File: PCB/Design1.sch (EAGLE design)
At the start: 23 parts, among them J1 FTDI_DEVICE, U1 ATMEGA2560AU

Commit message: Update new Schematic
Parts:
- added CHARGE: (no value), SparkFun-Connectors:M03X2FEMALE
- added D2: (no value), SparkFun-DiscreteSemi:DIODESMA-ALT
- added R4: 470KΩ, SparkFun-Resistors:RESISTOR1206
- added R5: 100KΩ, SparkFun-Resistors:RESISTOR1206
- 5V: value 7805T -> 7805
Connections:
- net SERIAL0 renamed TX1
- net SERIAL1 renamed RX1
- net SERIAL2 renamed TX2
- net SERIAL3 renamed RX2
- new net RAW: D2.A, POWER.2
- new net VSENSE: R4.2, R5.1
- net GND: now also CHARGE.2, CHARGE.6, R5.2
- net VIN: now also D2.C, R4.1; no longer POWER.2
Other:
- note added: "Power Source Mgmt"
- moved on the sheet: 5V, C1, C2, C6, POWER

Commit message: last nights' Schematic updates
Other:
- note added: "Reset circuitry"
- moved on the sheet: 5V, AMS1117, C1, C10, C2, C3, C4, C5, C6, C9, D1, D2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

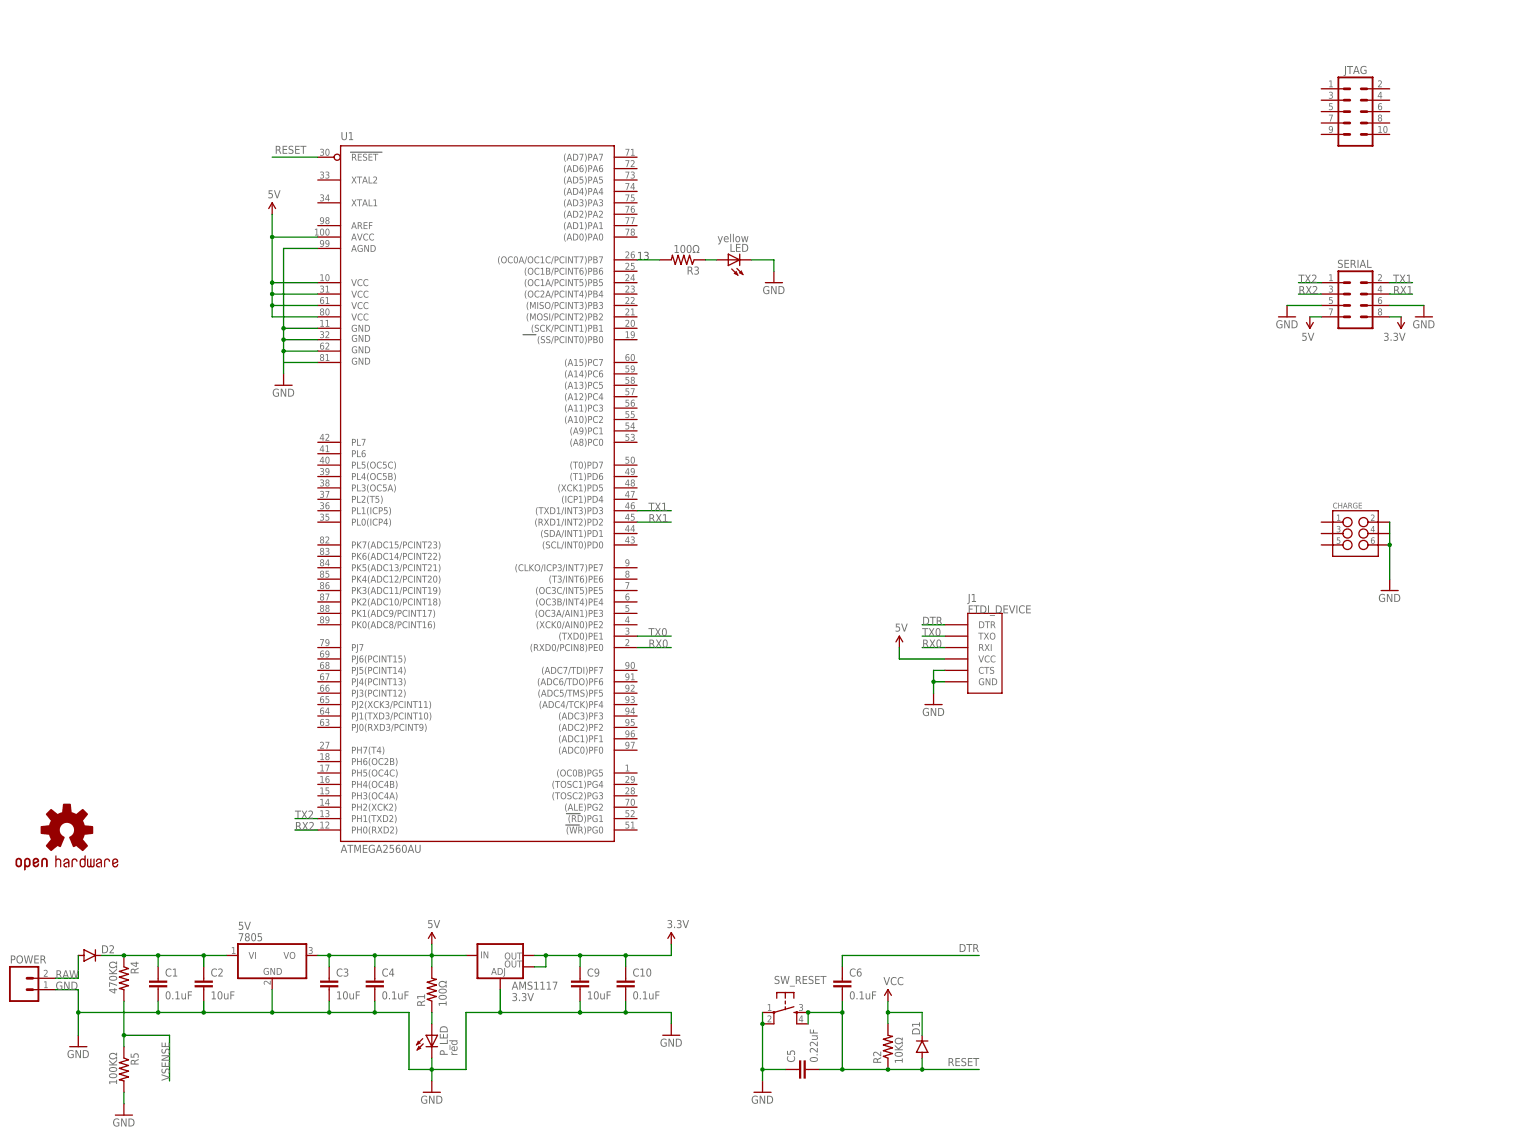
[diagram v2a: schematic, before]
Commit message: Add ICSP & Organize LEDs
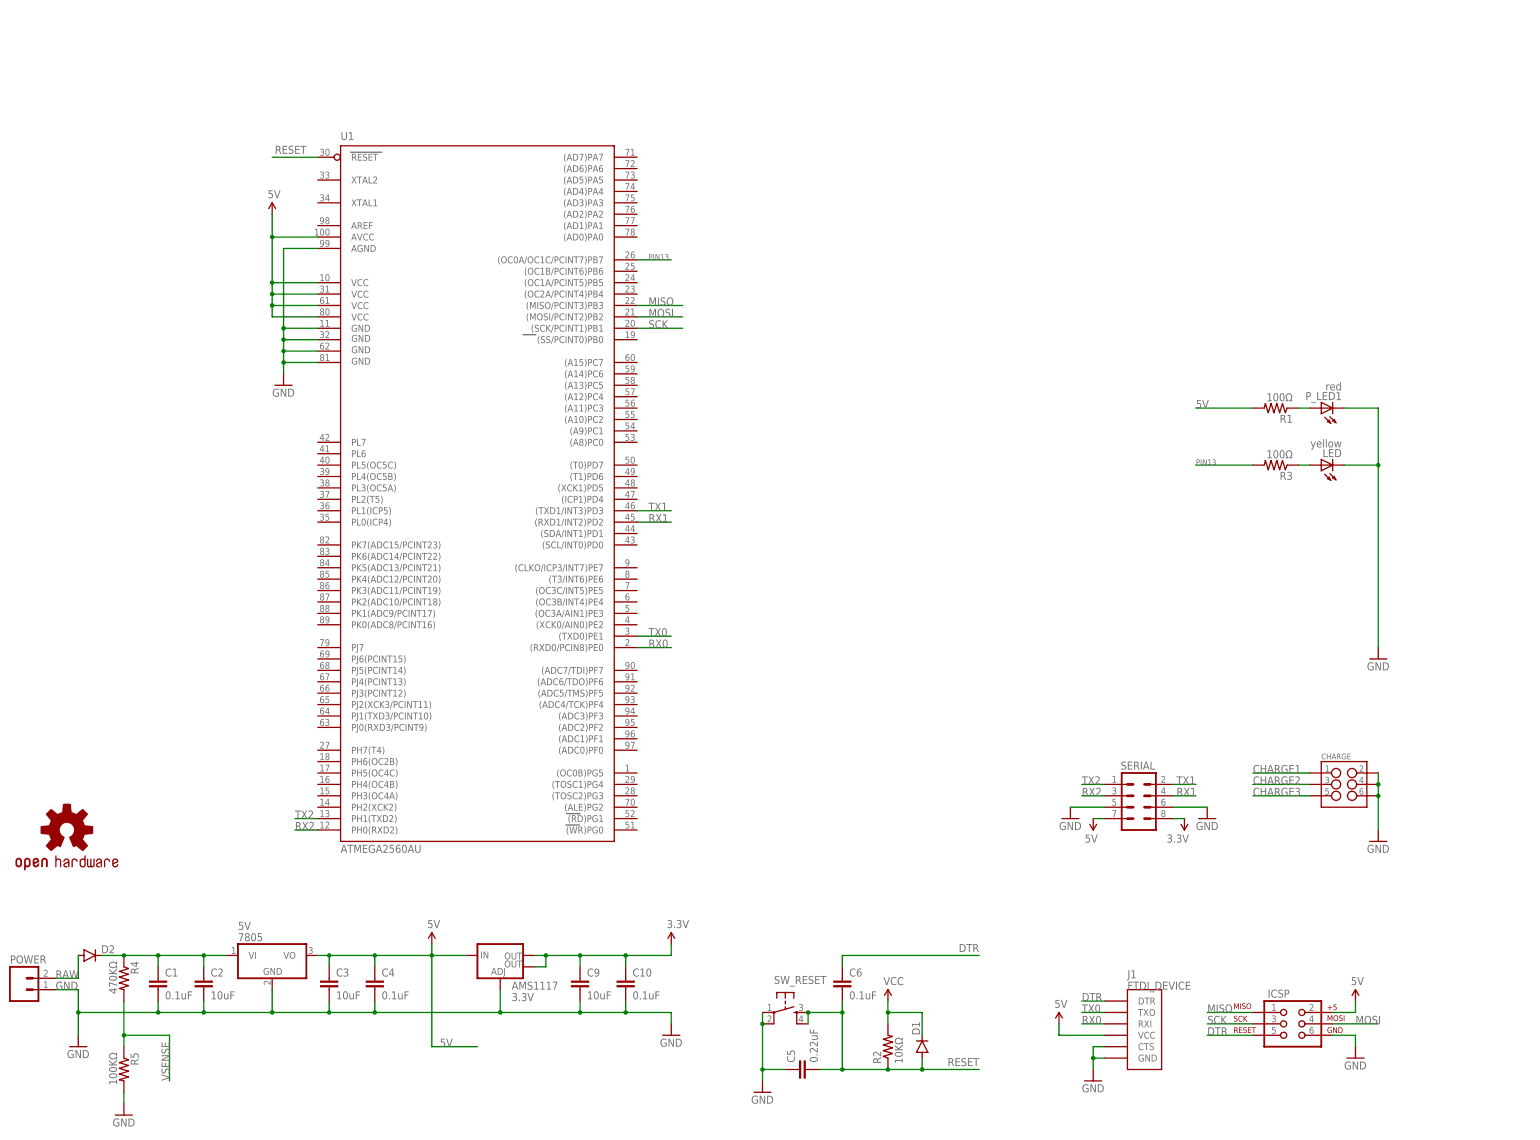
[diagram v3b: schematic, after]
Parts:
- removed JTAG: (no value), SparkFun-Connectors:M05X2PTH
- removed P_LED: red, led:LEDSML0805
- added ICSP: AVR_SPI_PRG_6PTH, SparkFun-Connectors:AVR_SPI_PRG_6PTH
- added P_LED1: red, led:LEDSML0805
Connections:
- removed net N$1: P_LED.A, R1.1
- new net CHARGE1: CHARGE.1
- new net CHARGE2: CHARGE.3
- new net CHARGE3: CHARGE.5
- new net MISO: ICSP.1, U1.(MISO/PCINT3)PB3
- new net MOSI: ICSP.4, U1.(MOSI/PCINT2)PB2
- new net N$2: P_LED1.A, R1.1
- new net SCK: ICSP.3, U1.(SCK/PCINT1)PB1
- net 5V: now also ICSP.2
- net DTR: now also ICSP.5
- net GND: now also CHARGE.4, ICSP.6, P_LED1.C; no longer P_LED.C
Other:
- note added: "(LED)"
- note added: "LEDs"
- note added: "Peripheral Connections"
- note added: "Programming Connections"
- note removed: "13"
- moved on the sheet: CHARGE, J1, LED, R1, R3, SERIAL

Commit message: Ad LEDS, begin work on MOSFETs
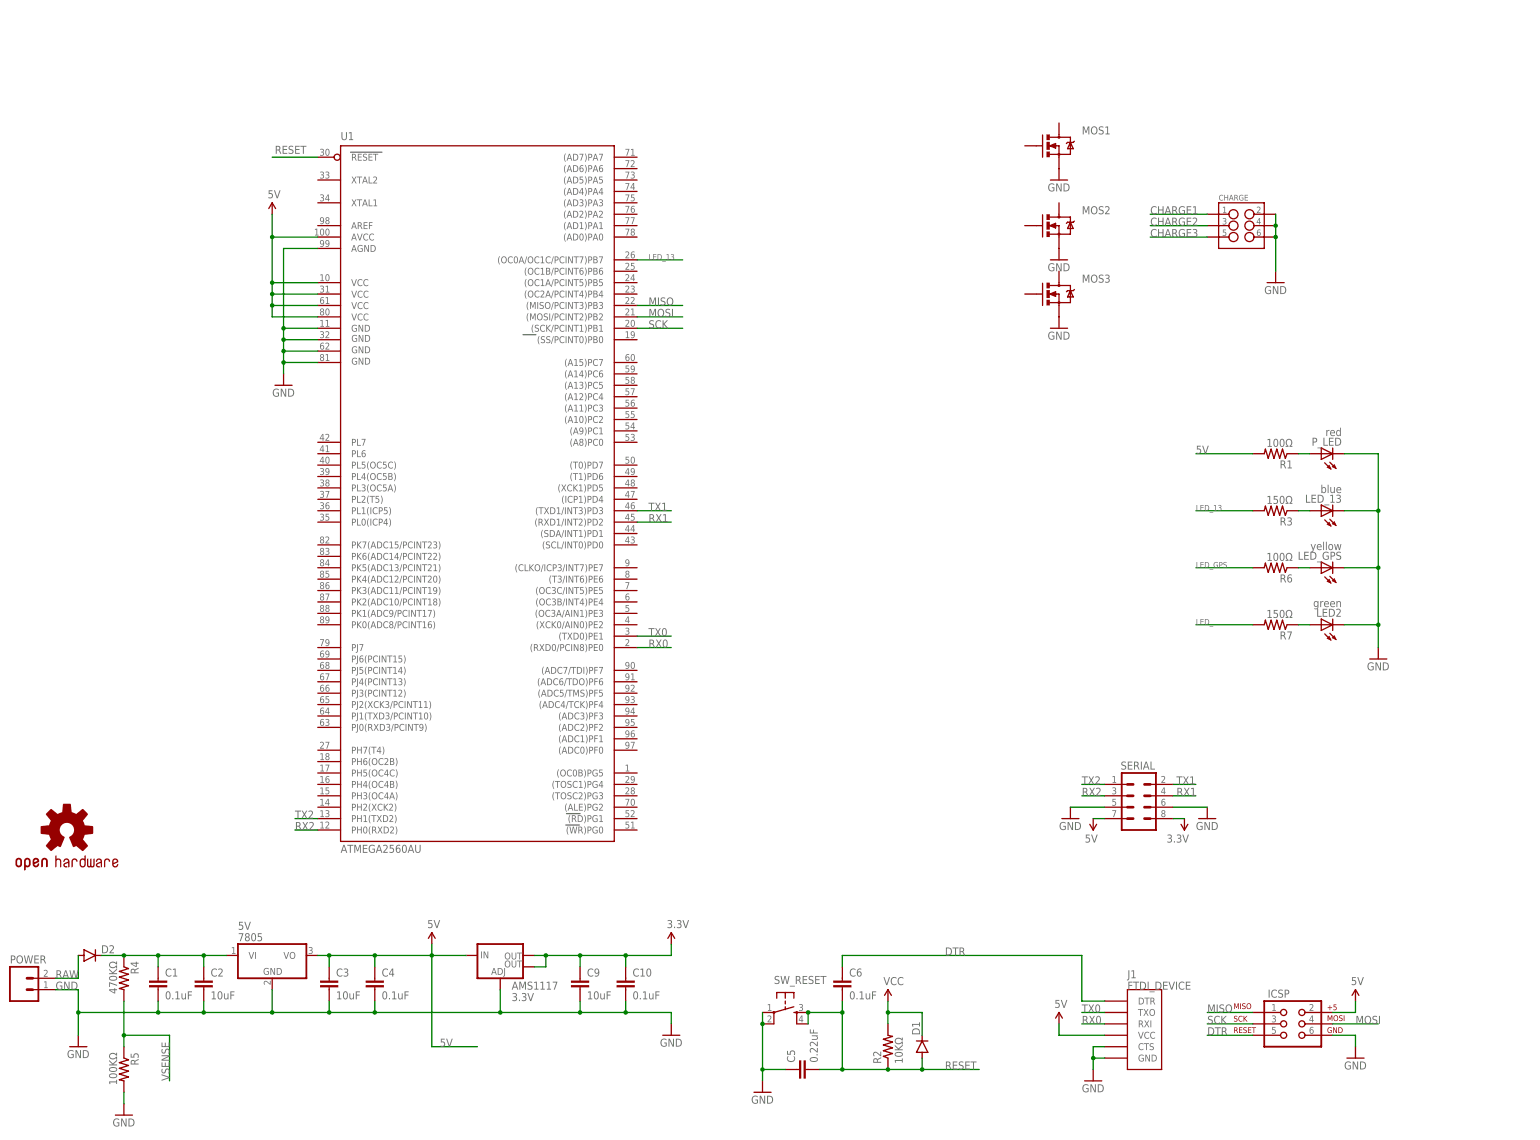
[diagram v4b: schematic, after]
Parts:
- removed LED: yellow, led:LEDSML0805
- removed P_LED1: red, led:LEDSML0805
- added LED2: green, led:LEDSML0805
- added LED_13: blue, led:LEDSML0805
- added LED_GPS: yellow, led:LEDSML0805
- added MOS1, MOS2, MOS3: MOSFET-NCHANNELFQP30N06L, SparkFun-DiscreteSemi:MOSFET-NCHANNELFQP30N06L
- added P_LED: red, led:LEDSML0805
- added R6: 100Ω, SparkFun-Resistors:RESISTOR1206
- added R7: 150Ω, SparkFun-Resistors:RESISTOR1206
- R3: value 100Ω -> 150Ω
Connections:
- net PIN13 renamed LED_13
- new net LED_: R7.2
- new net LED_GPS: R6.2
- new net N$1: LED_GPS.A, R6.1
- new net N$4: LED2.A, R7.1
- net GND: now also LED2.C, LED_13.C, LED_GPS.C, MOS1.S, MOS2.S, MOS3.S, P_LED.C; no longer LED.C, P_LED1.C
- net N$2: now also P_LED.A; no longer P_LED1.A
- net N$3: now also LED_13.A; no longer LED.A
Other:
- moved on the sheet: CHARGE, R1, R3

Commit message: Place mosfets
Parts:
- removed CHARGE: (no value), SparkFun-Connectors:M03X2FEMALE
- removed MOS3: MOSFET-NCHANNELFQP30N06L, SparkFun-DiscreteSemi:MOSFET-NCHANNELFQP30N06L
- added J2, J3: (no value), SparkFun-Connectors:M02LOCK_LONGPADS
- added R8, R9: 10KΩ, SparkFun-Resistors:RESISTOR1206
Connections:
- removed net CHARGE3: CHARGE.5
- removed net RAW: D2.A, POWER.2
- new net MOS1: J2.1, MOS1.D
- new net MOS2: J3.1, MOS2.D
- new net N$8: 5V.VI, C1.1, C2.1, D2.C, R4.1
- net CHARGE1: now also MOS1.G, R8.1; no longer CHARGE.1
- net CHARGE2: now also MOS2.G, R9.1; no longer CHARGE.3
- net GND: now also R8.2, R9.2; no longer CHARGE.2, CHARGE.4, CHARGE.6, MOS3.S
- net VIN: now also D2.A, J2.2, J3.2, POWER.2; no longer 5V.VI, C1.1, C2.1, D2.C, R4.1
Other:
- note added: "'Charge' MOSFET Switching"
- moved on the sheet: MOS1, MOS2

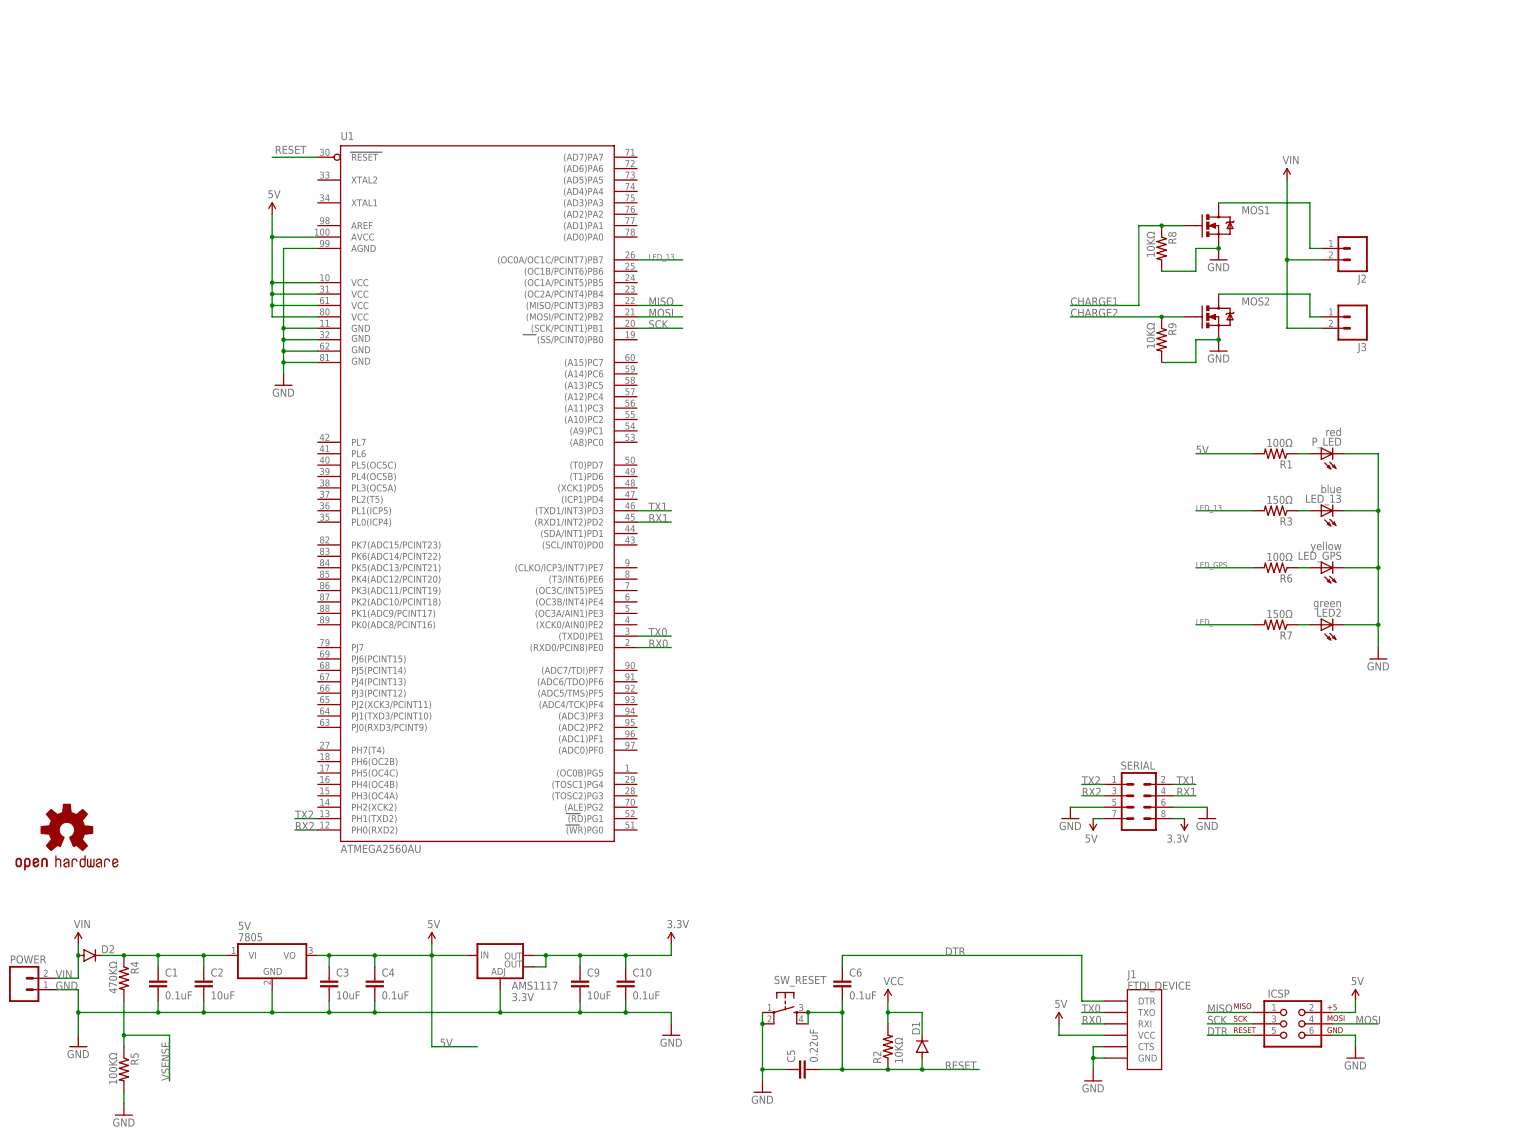
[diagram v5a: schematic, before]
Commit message: switch to SMT 5v regulators
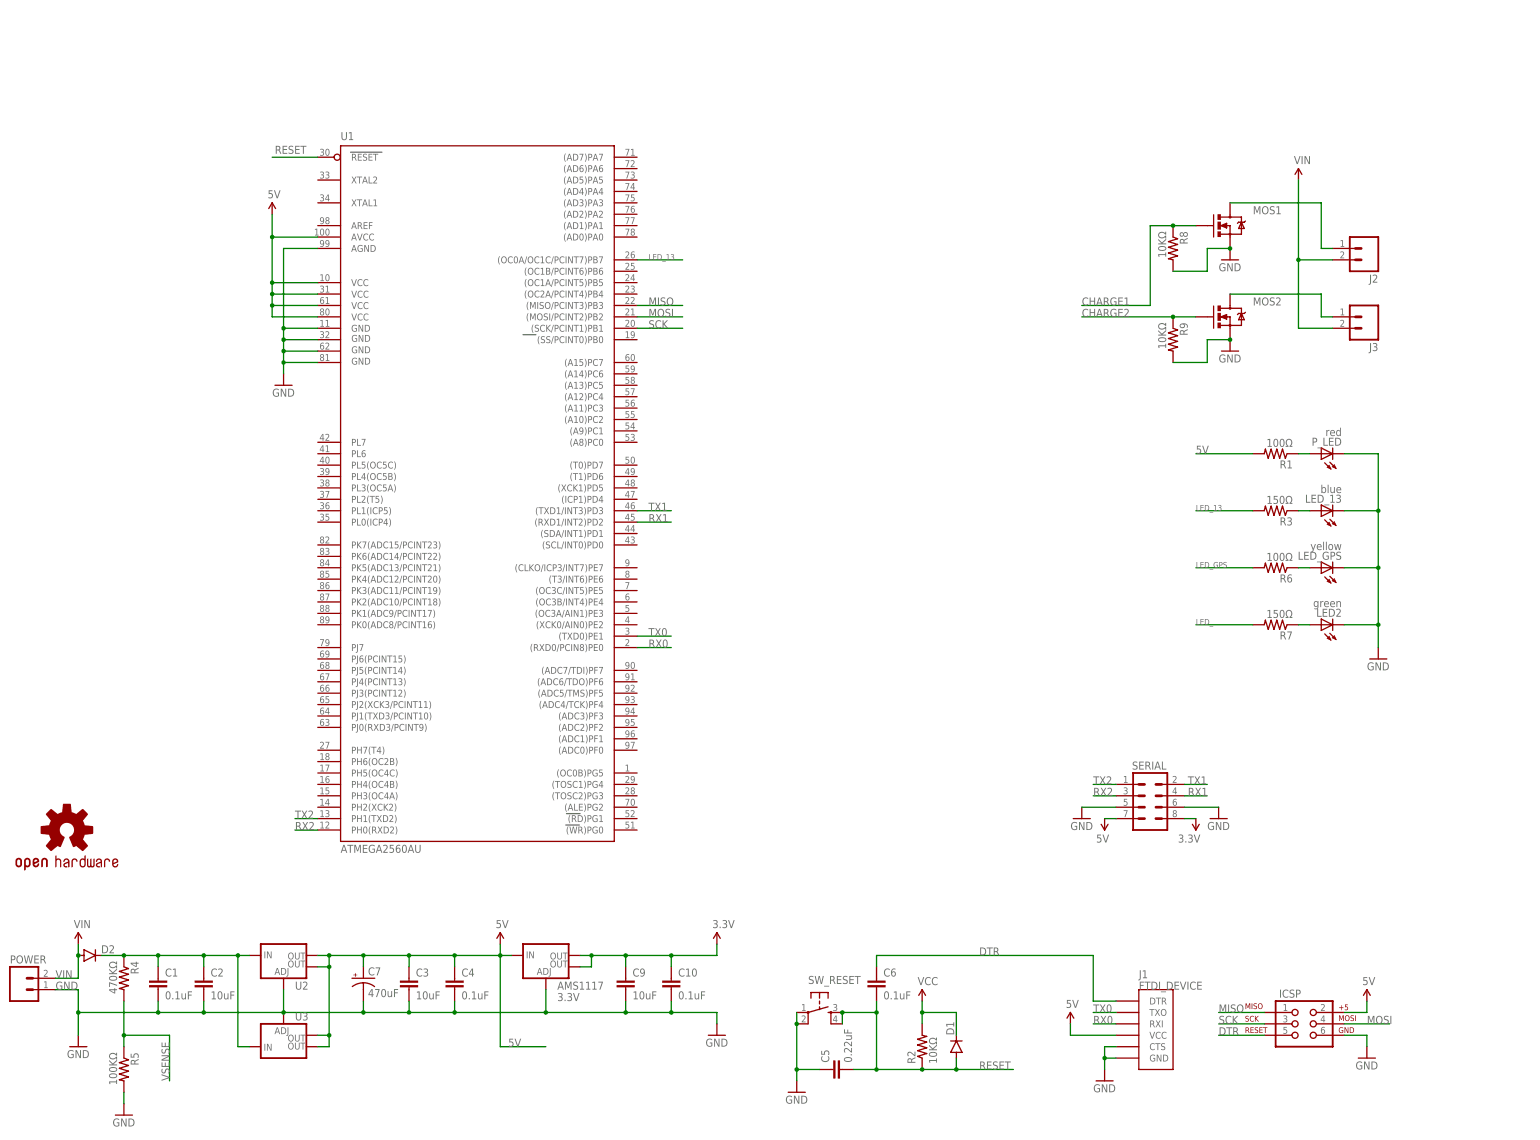
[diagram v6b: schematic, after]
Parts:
- removed 5V: 7805, linear:7805T
- added C7: 470uF, SparkFun-Capacitors:CAP_POLPTH1
- added U2, U3: (no value), SparkFun-PowerIC:V_REG_LM1117SOT223
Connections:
- net 5V: now also C7.+, U2.OUT, U2.OUT@1, U3.OUT, U3.OUT@1; no longer 5V.VO
- net GND: now also C7.-, U2.ADJ, U3.ADJ; no longer 5V.GND
- net N$8: now also U2.IN, U3.IN; no longer 5V.VI
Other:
- moved on the sheet: AMS1117, C10, C3, C4, C5, C6, C9, D1, ICSP, J1, J2, J3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
